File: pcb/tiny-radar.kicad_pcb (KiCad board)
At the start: 4 copper layers, 70 x 27.5 mm, 103 parts, among them P201 USB_OTG, P202 CONN_01X04, P203 CONN_01X04, P401 CONN_01X02, P402 CONN_01X02, SW201 SW_PUSH, SW202 SW_PUSH, U201 AP2114H, U202 STM32L432K, U301 AD8330AC, U302 LMX358IQ, U401 MAX2750, U402 MGA-635P8, U403 HHM1520, U404 MGA-635P8, U405 LT5560, U406 PD2328J, U407 WA04P

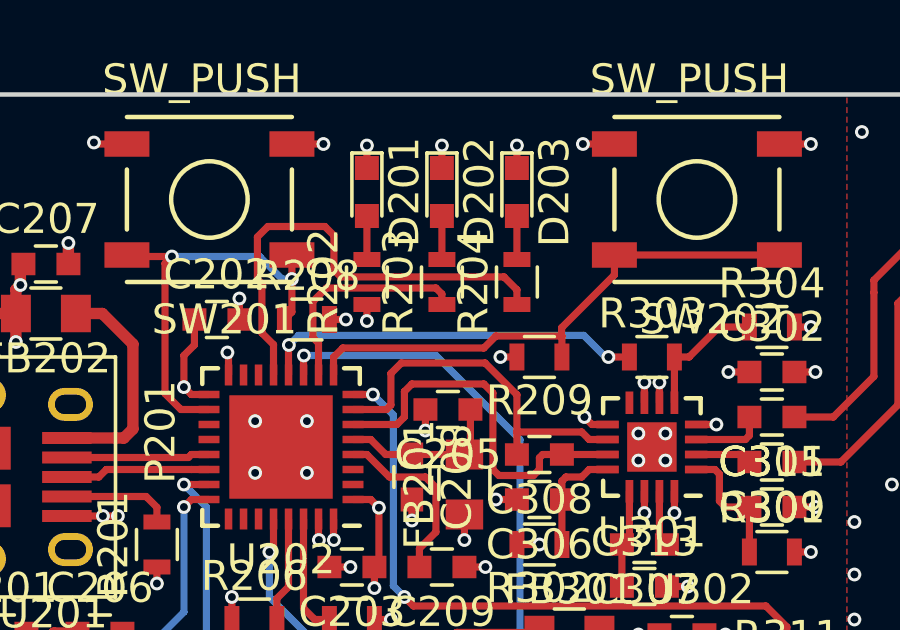
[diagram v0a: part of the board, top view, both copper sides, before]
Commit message: fixed DAC pin swap on radar board
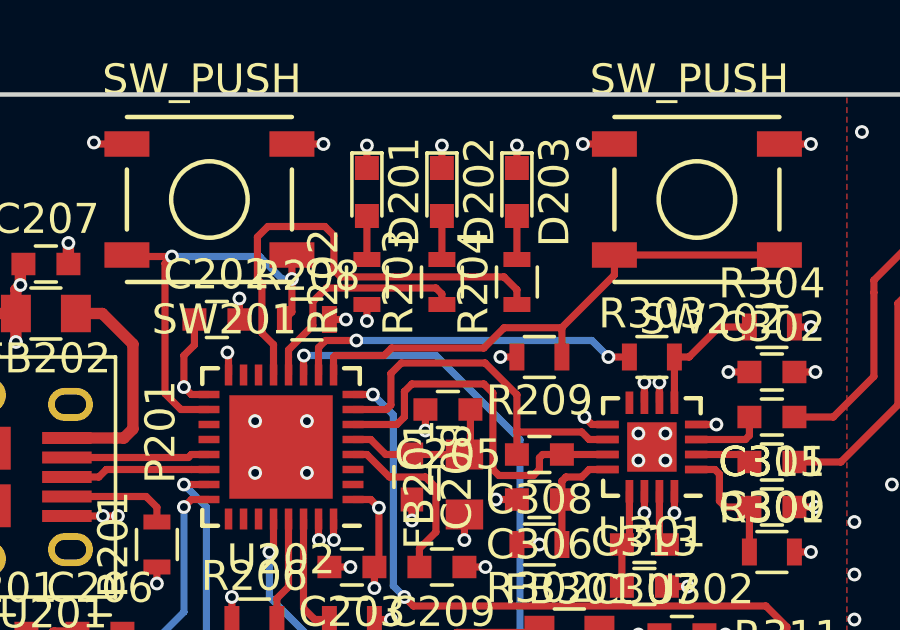
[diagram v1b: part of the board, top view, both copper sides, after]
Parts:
- C307, C309, C311: value C -> 3.3u
- C308: value C -> 47n
- C406: value C -> 1n
- L403: value 2.2n -> 2.7n
- R301, R302: value R -> 4.7
- R303, R304: value R -> 4.7K
- R404: value R -> 3
- R408, R409: value R -> 200
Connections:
- U202 pad 10: /Control/STATUS_1 -> /Control/AGC_DAC
- U202 pad 12: /Control/AGC_DAC -> /Control/STATUS_1
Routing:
- net /Control/AGC_DAC: track 12.8 -> 11.7 mm
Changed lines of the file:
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@@
-(kicad_pcb (version 4) (host pcbnew 4.0.5-e0-6337~49~ubuntu14.04.1)
+(kicad_pcb (version 4) (host pcbnew 4.0.6-e0-6349~53~ubuntu14.04.1)
   (general
     (links 242)
-    (no_connects 0)
-    (area 138.425 62.345 213.963334 94.305)
+    (no_connects 2)
+    (area 141.924999 63.924999 212.075001 91.575001)
     (thickness 1.6)
     (drawings 5)
-    (tracks 1144)
+    (tracks 1146)
     (zones 0)
     (modules 103)
@@
   )
   (setup
-    (last_trace_width 0.13)
+    (last_trace_width 0.24)
     (user_trace_width 0.13)
     (user_trace_width 0.24)
@@
       (net 65 /Control/BUTTON_2))
     (pad 10 smd rect (at -1.25 2.4 270) (size 0.7 0.25) (layers F.Cu F.Paste F.Mask)
-      (net 53 /Control/STATUS_1))
+      (net 66 /Control/AGC_DAC))
     (pad 11 smd rect (at -0.75 2.4 270) (size 0.7 0.25) (layers F.Cu F.Paste F.Mask)
       (net 52 /Analog/RAMP_DAC))
     (pad 12 smd rect (at -0.25 2.4 270) (size 0.7 0.25) (layers F.Cu F.Paste F.Mask)
-      (net 66 /Control/AGC_DAC))
+      (net 53 /Control/STATUS_1))
     (pad 13 smd rect (at 0.25 2.4 270) (size 0.7 0.25) (layers F.Cu F.Paste F.Mask)
       (net 54 /Control/STATUS_2))
@@
       (effects (font (size 1 1) (thickness 0.15)))
     )
-    (fp_text value C (at 0 1.5 180) (layer F.Fab)
+    (fp_text value 3.3u (at 0 1.5 180) (layer F.Fab)
       (effects (font (size 1 1) (thickness 0.15)))
     )
@@
       (effects (font (size 1 1) (thickness 0.15)))
     )
-    (fp_text value C (at 0 1.5 180) (layer F.Fab)
+    (fp_text value 47n (at 0 1.5 180) (layer F.Fab)
       (effects (font (size 1 1) (thickness 0.15)))
     )
@@
       (effects (font (size 1 1) (thickness 0.15)))
     )
-    (fp_text value C (at 0 1.5 180) (layer F.Fab)
+    (fp_text value 3.3u (at 0 1.5 180) (layer F.Fab)
       (effects (font (size 1 1) (thickness 0.15)))
     )
@@
       (effects (font (size 1 1) (thickness 0.15)))
     )
-    (fp_text value C (at 0 1.5 180) (layer F.Fab)
+    (fp_text value 3.3u (at 0 1.5 180) (layer F.Fab)
       (effects (font (size 1 1) (thickness 0.15)))
     )
@@
       (effects (font (size 1 1) (thickness 0.15)))
     )
-    (fp_text value 2.2n (at 0 1.27 180) (layer F.Fab)
+    (fp_text value 2.7n (at 0 1.27 180) (layer F.Fab)
       (effects (font (size 1 1) (thickness 0.15)))
     )
@@
       (effects (font (size 1 1) (thickness 0.15)))
     )
-    (fp_text value R (at 0 1.5) (layer F.Fab)
+    (fp_text value 4.7 (at 0 1.5) (layer F.Fab)
       (effects (font (size 1 1) (thickness 0.15)))
     )
@@
       (effects (font (size 1 1) (thickness 0.15)))
     )
-    (fp_text value R (at 0 1.5 180) (layer F.Fab)
+    (fp_text value 4.7 (at 0 1.5 180) (layer F.Fab)
       (effects (font (size 1 1) (thickness 0.15)))
     )
@@
       (effects (font (size 1 1) (thickness 0.15)))
     )
-    (fp_text value R (at 0 1.5) (layer F.Fab)
+    (fp_text value 4.7K (at 0 1.5) (layer F.Fab)
       (effects (font (size 1 1) (thickness 0.15)))
     )
@@
       (effects (font (size 1 1) (thickness 0.15)))
     )
-    (fp_text value R (at 0 1.5) (layer F.Fab)
+    (fp_text value 4.7K (at 0 1.5) (layer F.Fab)
       (effects (font (size 1 1) (thickness 0.15)))
     )
@@
       (effects (font (size 1 1) (thickness 0.15)))
     )
-    (fp_text value R (at 0 1.45) (layer F.Fab)
+    (fp_text value 3 (at 0 1.45) (layer F.Fab)
       (effects (font (size 1 1) (thickness 0.15)))
     )
@@
       (effects (font (size 1 1) (thickness 0.15)))
     )
-    (fp_text value R (at 0 1.45 270) (layer F.Fab)
+    (fp_text value 200 (at 0 1.45 270) (layer F.Fab)
       (effects (font (size 1 1) (thickness 0.15)))
     )
@@
       (effects (font (size 1 1) (thickness 0.15)))
     )
-    (fp_text value R (at 0 1.45 90) (layer F.Fab)
+    (fp_text value 200 (at 0 1.45 90) (layer F.Fab)
       (effects (font (size 1 1) (thickness 0.15)))
     )
@@
       (effects (font (size 1 1) (thickness 0.15)))
     )
-    (fp_text value C (at 0 1.27 180) (layer F.Fab)
+    (fp_text value 1n (at 0 1.27 180) (layer F.Fab)
       (effects (font (size 1 1) (thickness 0.15)))
     )
@@
   (segment (start 166.625 84.75) (end 166.05 84.75) (width 0.24) (layer F.Cu) (net 52))
   (via (at 166.05 84.75) (size 0.46) (drill 0.26) (layers F.Cu B.Cu) (net 52))
+  (segment (start 155.2 70.899998) (end 155.2 71.700002) (width 0.24) (layer F.Cu) (net 53))
+  (segment (start 155.2 71.700002) (end 154.3875 72.512502) (width 0.24) (layer F.Cu) (net 53))
+  (segment (start 154.3875 72.512502) (end 154.3875 72.76) (width 0.24) (layer F.Cu) (net 53))
+  (segment (start 154.3875 72.76) (end 154.3875 73.35) (width 0.24) (layer F.Cu) (net 53))
   (segment (start 159.5 71) (end 159.5 70.65) (width 0.24) (layer F.Cu) (net 53))
-  (segment (start 155.2 70.899998) (end 155.2 72.1) (width 0.24) (layer F.Cu) (net 53))
   (segment (start 159.5 70.65) (end 159.3 70.45) (width 0.24) (layer F.Cu) (net 53))
   (segment (start 159.3 70.45) (end 155.649998 70.45) (width 0.24) (layer F.Cu) (net 53))
   (segment (start 155.649998 70.45) (end 155.2 70.899998) (width 0.24) (layer F.Cu) (net 53))
-  (segment (start 155.2 72.1) (end 155.3875 72.2875) (width 0.24) (layer F.Cu) (net 53))
-  (segment (start 155.3875 72.2875) (end 155.3875 73.35) (width 0.24) (layer F.Cu) (net 53))
   (segment (start 153.8875 73.35) (end 153.8875 72.3375) (width 0.24) (layer F.Cu) (net 54))
   (segment (start 153.8875 72.3375) (end 153.499999 71.949999) (width 0.24) (layer F.Cu) (net 54))
@@
   (via (at 154.5 70.15) (size 0.46) (drill 0.26) (layers F.Cu B.Cu) (net 64))
   (segment (start 154.5 71.25) (end 154.25 71.5) (width 0.24) (layer F.Cu) (net 64))
-  (segment (start 170.75 69.35) (end 165.25 69.35) (width 0.24) (layer F.Cu) (net 65))
-  (segment (start 165.25 69.35) (end 165.25 70.015) (width 0.24) (layer F.Cu) (net 65))
-  (segment (start 165.25 70.015) (end 163.489999 71.775001) (width 0.24) (layer F.Cu) (net 65))
-  (segment (start 163.489999 71.775001) (end 163.489999 72.049999) (width 0.24) (layer F.Cu) (net 65))
+  (segment (start 163.489999 71.775001) (end 163.5 71.785002) (width 0.24) (layer F.Cu) (net 65))
+  (segment (start 163.5 71.785002) (end 163.5 72.75) (width 0.24) (layer F.Cu) (net 65))
   (segment (start 155.8875 73.35) (end 155.8875 72.76) (width 0.24) (layer F.Cu) (net 65))
-  (segment (start 155.8875 72.76) (end 156.1975 72.45) (width 0.24) (layer F.Cu) (net 65))
-  (segment (start 156.1975 72.45) (end 160.9 72.45) (width 0.24) (layer F.Cu) (net 65))
-  (segment (start 160.9 72.45) (end 161.300001 72.049999) (width 0.24) (layer F.Cu) (net 65))
-  (segment (start 163.489999 72.049999) (end 163.5 72.06) (width 0.24) (layer F.Cu) (net 65))
-  (segment (start 161.300001 72.049999) (end 163.489999 72.049999) (width 0.24) (layer F.Cu) (net 65))
-  (segment (start 163.5 72.06) (end 163.5 72.75) (width 0.24) (layer F.Cu) (net 65))
+  (segment (start 155.8875 72.76) (end 155.9475 72.7) (width 0.24) (layer F.Cu) (net 65))
+  (segment (start 155.9475 72.7) (end 157.575 72.7) (width 0.24) (layer F.Cu) (net 65))
+  (segment (start 165.25 70.015) (end 165.25 69.35) (width 0.24) (layer F.Cu) (net 65))
+  (segment (start 157.575 72.7) (end 157.825 72.45) (width 0.24) (layer F.Cu) (net 65))
+  (segment (start 157.825 72.45) (end 160.9 72.45) (width 0.24) (layer F.Cu) (net 65))
+  (segment (start 160.9 72.45) (end 161.574999 71.775001) (width 0.24) (layer F.Cu) (net 65))
+  (segment (start 161.574999 71.775001) (end 163.489999 71.775001) (width 0.24) (layer F.Cu) (net 65))
+  (segment (start 163.489999 71.775001) (end 165.25 70.015) (width 0.24) (layer F.Cu) (net 65))
+  (segment (start 170.75 69.35) (end 165.25 69.35) (width 0.24) (layer F.Cu) (net 65))
+  (segment (start 156.65 72.2) (end 164.5 72.2) (width 0.24) (layer B.Cu) (net 66))
+  (segment (start 164.5 72.2) (end 165.05 72.75) (width 0.24) (layer B.Cu) (net 66))
+  (segment (start 155.625 72.2) (end 156.65 72.2) (width 0.24) (layer F.Cu) (net 66))
+  (via (at 156.65 72.2) (size 0.46) (drill 0.26) (layers F.Cu B.Cu) (net 66))
+  (segment (start 155.3875 72.4375) (end 155.625 72.2) (width 0.24) (layer F.Cu) (net 66))
+  (segment (start 155.3875 73.35) (end 155.3875 72.4375) (width 0.24) (layer F.Cu) (net 66))
   (segment (start 165.05 72.75) (end 165.75 72.75) (width 0.24) (layer F.Cu) (net 66))
-  (segment (start 164.230001 72.030001) (end 164.95 72.75) (width 0.24) (layer B.Cu) (net 66))
   (segment (start 164.95 72.75) (end 165.05 72.75) (width 0.24) (layer B.Cu) (net 66))
   (via (at 165.05 72.75) (size 0.46) (drill 0.26) (layers F.Cu B.Cu) (net 66))
-  (segment (start 154.399602 72.349765) (end 154.719366 72.030001) (width 0.24) (layer B.Cu) (net 66))
-  (segment (start 154.719366 72.030001) (end 164.230001 72.030001) (width 0.24) (layer B.Cu) (net 66))
-  (segment (start 154.3875 73.35) (end 154.3875 72.361867) (width 0.24) (layer F.Cu) (net 66))
-  (segment (start 154.3875 72.361867) (end 154.399602 72.349765) (width 0.24) (layer F.Cu) (net 66))
-  (via (at 154.399602 72.349765) (size 0.46) (drill 0.26) (layers F.Cu B.Cu) (net 66))
   (segment (start 168.74 71.75) (end 169.75 71.75) (width 0.24) (layer F.Cu) (net 67))
   (segment (start 167.25 72.75) (end 167.74 72.75) (width 0.24) (layer F.Cu) (net 67))

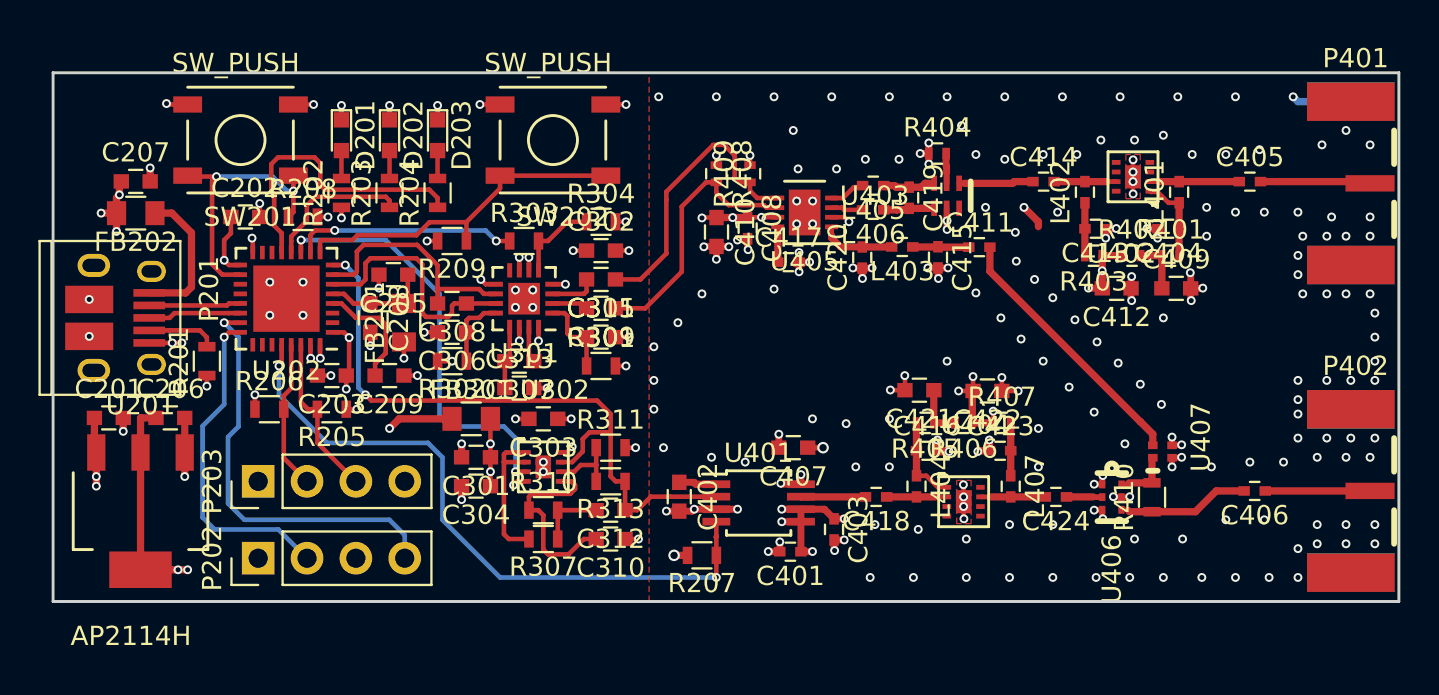
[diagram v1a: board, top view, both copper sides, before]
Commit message: added PA board
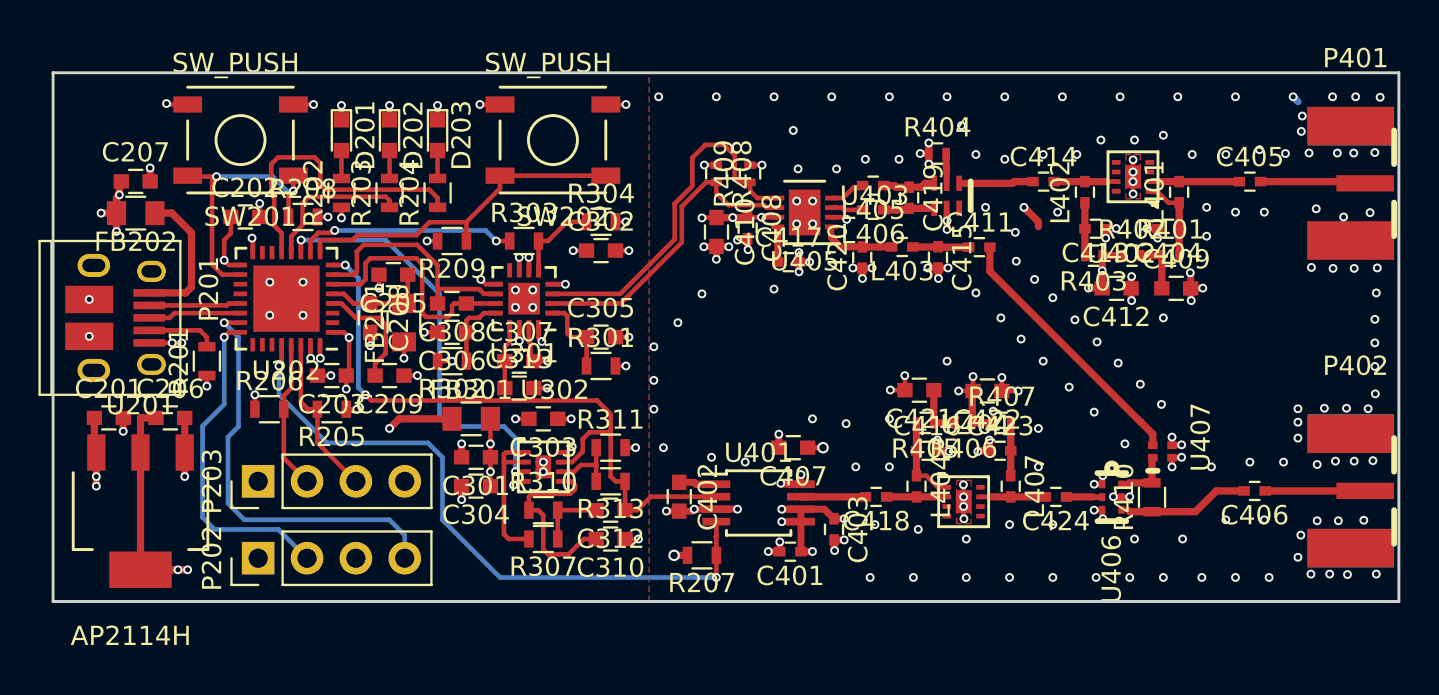
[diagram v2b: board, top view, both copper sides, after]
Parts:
- removed C309, C311: 3.3u, Capacitors_SMD:C_0603
- P401, P402: footprint wbraun_smd:SMA-Edge-short -> wbraun_smd:SMA-Edge-China-Short
- turned C307 to 0 degrees
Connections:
- C307 pad 2: Net-(C307-Pad2) -> GND
- C313 pad 1: Net-(C307-Pad2) -> Net-(C307-Pad1)
- C408 pad 1: +5V -> +3V3
- C410 pad 1: +5V -> +3V3
- R408 pad 1: +5V -> +3V3
- R409 pad 2: +5V -> +3V3
- U301 pad 13: Net-(C307-Pad2) -> Net-(C307-Pad1)
- U301 pad 15: Net-(C307-Pad1) -> GND
- U301 pad 2: Net-(C309-Pad2) -> /Analog/IF+
- U301 pad 3: Net-(C311-Pad2) -> /Analog/IF-
- U405 pad 2: +5V -> +3V3
- U405 pad 7: +5V -> +3V3
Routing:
- net GND: track 400.3 -> 441.9 mm, vias 248 -> 250
- net +3V3: track 30.1 -> 36.1 mm, vias 16 -> 22
- net +5V: track 24.9 -> 19.0 mm, vias 17 -> 11
- net /Analog/IF-: track 15.4 -> 19.0 mm
- net Net-(C307-Pad2): track 3.53 -> 0.00 mm
- net Net-(C311-Pad2): track 2.45 -> 0.00 mm
- net /Analog/IF+: track 14.0 -> 16.3 mm
- net Net-(C309-Pad2): track 1.88 -> 0.00 mm
- net Net-(C307-Pad1): track 2.13 -> 3.28 mm
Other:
- board text added: "μRadar V1.1 wbraun@mit.edu"
- board text removed: "μRadar V1.0 wbraun@mit.edu"
